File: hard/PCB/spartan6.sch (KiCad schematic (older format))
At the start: 18 parts, among them IC1 W9812G6KH, P1 CONN_02X20, U1 XC6SLX9-2TQG144C

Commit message: ok lvds  and hdmi
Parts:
- removed RS5: 4.7k, Resistors_SMD:R_0603, symbol R
- added DS3: LED, LEDs:LED_0603, symbol LED-RESCUE-i.MX283_Board
- added RR2, RR3: 47k, Resistors_SMD:R_0603, symbol R
- added U6: S25FL064LABMFI013, SMD_Packages:SOIC-8-N, symbol 25LC_EEPROM
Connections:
- net labels added: CH1_N, CH1_P, CH2_N, CH2_P, CH3_N, CH3_P, CH4_N, CH4_P, CLK_N, CLK_P, DONE, FPGA_CLK_IN, FPGA_CLK_OUT, HDMI, INIT_B, LVDS, MEMORY_SPI_CS, MEMORY_SPI_MISO, MEMORY_SPI_MOSI, MEMORY_SPI_SCK
- net labels removed: CH1N, CH1P, CH2N, CH2P, CH3N, CH3P, CH4N, CH4P, CLKN, CLKP, FPGA_CK
- wire segments 298 -> 315
- no-connect marks 12 -> 10
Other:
- note added: "pin 144 \ngnd for pull_up in soft \nvcc for pull_up in hw"
- moved on the sheet: HDMI1, LVDS1, RN1, RR1, RS1, RS2, RS3, RS4, RST1, U1, XS1

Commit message: Changes in HDMISpartan6_Board
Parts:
- removed IC1: W9812G6KH, Project:TSOPII54_SDRAM_MT48, symbol MT48LC4M16A2P
- added P3: CONN_01X03, Pin_Headers:Pin_Header_Straight_1x03_Pitch2.54mm, symbol CONN_01X03
- added R10, R11, R12, R13, R2, R3, R4, R5, R6, R7, R8, R9: 0, Resistors_SMD:R_0603, symbol R
- added XS2: uSD CARD, Project:Conn_uSDcard, symbol TFP09-2-12B
- RR1, RR3: value 47k -> 4.7k
- RR2: value 47k -> 330
- RST1: footprint Buttons_Switches_SMD:SW_SPST_B3SL-1002P -> Buttons_Switches_SMD:SW_SPST_KMR2; REF DIGIKEY SW1064CT-ND -> KMR211NG LFS (MOURSE)
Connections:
- net labels added: CCLK, Din, Dout, M0, M1, RpCS, RpDONE, RpGPIO_04, RpGPIO_08, RpGPIO_17, RpGPIO_18, RpGPIO_23, RpGPIO_24, RpGPIO_27, RpID_SC, RpINIT_B, RpMISO, RpMOSI, RpPROG, RpRXD, RpSCK, RpSCL, RpSDA, RpTXD, adCLK, adCS, adDA0, adDA1, adDA2, adDA3, adDA4, adDA5, adDA6, adDA7, adDA[0..7], adDD0, adDD1, adDD2, adDD3, adDD4, adDD5, adDD6, adDD7, adDD8, adDD9, adDD[0..9], adMOSI, adSCK, sCS, sMISO, sMOSI, sSCK, uD0, uD1, uD2, uD3, uD4, uD5, uD6, uD7, uD8, uD9, uDONE, uD[0..9], uINIT_B, uM0SI, uMISO, uP0, uP1, uP2, uP3, uP4, uP5, uP6, uPROG, uP[0..6], uSCK, uSS, usCD, usCS, usMISO, usMOSI, usSCK
- net labels removed: A0, A1, A10, A11, A2, A3, A4, A5, A6, A7, A8, A9, BA0, BA1, CKE, CLK, CS_AD, DA0, DA1, DA2, DA3, DA4, DA5, DA6, DA7, DA[0..7], DD0, DD1, DD2, DD3, DD4, DD5, DD6, DD7, DD8, DD9, DD[0..9], DQ0, DQ1, DQ10, DQ11, DQ12, DQ13, DQ14, DQ15, DQ2, DQ3, DQ4, DQ5, DQ6, DQ7, DQ8, DQ9, DQMH, DQML, FPGA_CLK_IN, FPGA_CLK_OUT, MEMORY_SPI_CS, MEMORY_SPI_MISO, MEMORY_SPI_MOSI, MEMORY_SPI_SCK, RXD, SCL, SDA, SPI_MISO, SPI_MOSI, SPI_SCK, TXD, ~CAS, ~CS, ~RAS, ~WE
- wire segments 315 -> 310
- no-connect marks 10 -> 12
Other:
- note added: "CMPCS_B_2 Reserved. Leave unconnected or connect High"
- note added: "I2C: SCL\n"
- note added: "I2C: SDA\n"
- note added: "M[1:0] | Mode CCLK Direction\n 01 | Master Serial/SPI Output\n 11 | Slave Serial Input\n 00 | Master SelectMAP Output -> not implement\n 10 | Slave SelectMAP Input ->not implement"
- note added: "PROG: CCLK"
- note added: "PROG: SERIAL_OUT"
- note added: "REVISAR!!!!!\n\nel reset del micro"
- note added: "TEMPORAL"
- note added: "cambio adDA6 y AdDA7\n para conexión en pcb"
- note added: "notas:\nFALTA CONECTAR:\nPIN RESET rst_um DE MICRO\n- uSS \n- LED1\n- LED2\n- micro SD\n"
- note removed: "REVISAR!!!!!"
- moved on the sheet: DS1, DS2, DS3, P1, RN1, RR1, RR2, RR3, RS6, RS7, RST1, U6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

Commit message: versión 1.0
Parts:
- renumbered DS3 to LED1, DS2 to LED2, DS1 to LED3
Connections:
- net labels added: RpGPIO_05, RpGPIO_06, RpGPIO_12, RpGPIO_13, RpGPIO_16, RpGPIO_19, RpGPIO_20, RpGPIO_21, RpGPIO_26, RpID_SD, rst_um
- net labels removed: RpGPIO_24
- wire segments 310 -> 317
- no-connect marks 12 -> 33
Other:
- note removed: ">>> F A L T A ! ! !\nAsignar a la FPGA"
- note removed: "REVISAR!!!!!\n\nel reset del micro"
- note removed: "TEMPORAL"
- note removed: "notas:\nFALTA CONECTAR:\nPIN RESET rst_um DE MICRO\n- uSS \n- LED1\n- LED2\n- micro SD\n"
- moved on the sheet: LED2, LED3, RS6, RS7

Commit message: silkS progresing
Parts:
- B1: renamed from RST1; value B3SL-1002P -> KMR211NG LFS; REF DIGIKEY KMR211NG LFS (MOURSE) -> KMR211NG LFS (MOUSER)
- renumbered LVDS1 to J1, HDMI1 to J3
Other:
- note added: "LVDS\n"

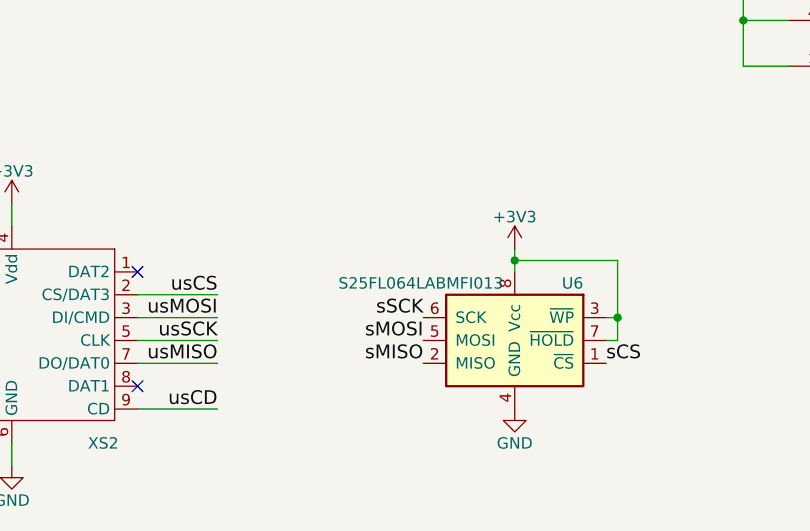
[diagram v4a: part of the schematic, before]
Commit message: cambio de la memoria flash, referecnia y encapsulado
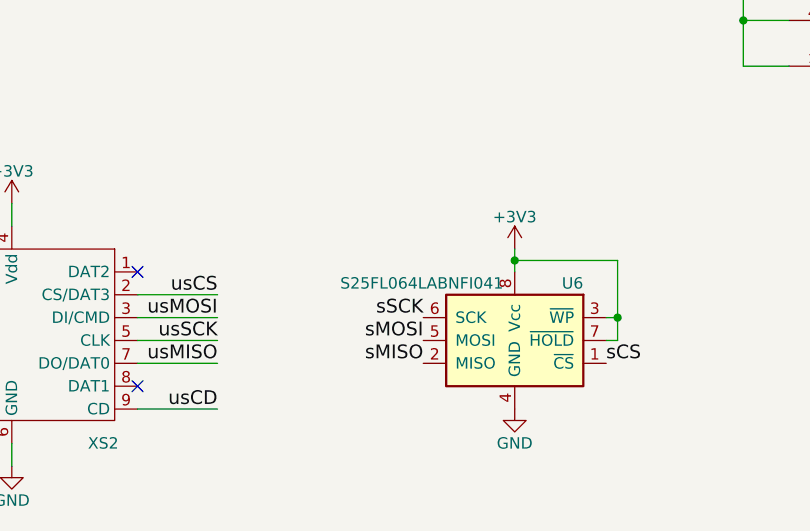
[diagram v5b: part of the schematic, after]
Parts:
- U6: value S25FL064LABMFI013 -> S25FL064LABNFI041; footprint SMD_Packages:SOIC-8-N -> Housings_DFN_QFN:DFN-8-1EP_4x4mm_Pitch0.8mm; DIGIKEY REF 428-4073-2-ND -> (none); Mouser REF (none) -> 727-S25FL064LANFI041
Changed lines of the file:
@@
 P 10550 9050
 F 0 "U6" H 10250 9300 50  0000 L CNN
-F 1 "S25FL064LABMFI013" H 10600 9300 50  0000 L CNN
-F 2 "SMD_Packages:SOIC-8-N" H 10200 9000 50  0001 C CNN
+F 1 "S25FL064LABNFI041" H 10600 9300 50  0000 L CNN
+F 2 "Housings_DFN_QFN:DFN-8-1EP_4x4mm_Pitch0.8mm" H 10200 9000 50  0001 C CNN
 F 3 "http://www.mouser.com/ds/2/100/002-12878_S25FL064L_64-Mbit_8-Mbyte_3.0_V_FL-L_SPI-1102570.pdf" H 10200 9000 50  0001 C CNN
-F 4 "428-4073-2-ND" H 10550 9050 60  0001 C CNN "DIGIKEY REF"
+F 4 "727-S25FL064LANFI041 " H 10550 9050 60  0001 C CNN "Mouser REF"
 	1    10550 9050
 	-1   0    0    -1
